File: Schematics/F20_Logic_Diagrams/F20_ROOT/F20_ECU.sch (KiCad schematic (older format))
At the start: 2 parts

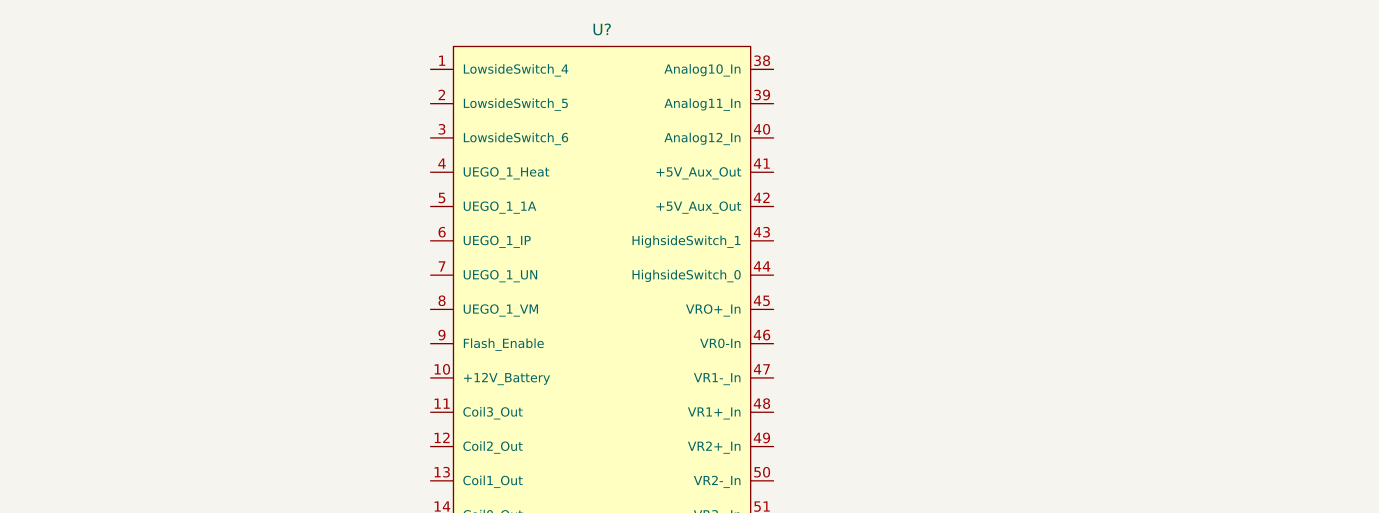
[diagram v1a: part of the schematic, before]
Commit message: Weekly update. Added Tire temp sensors drawing.
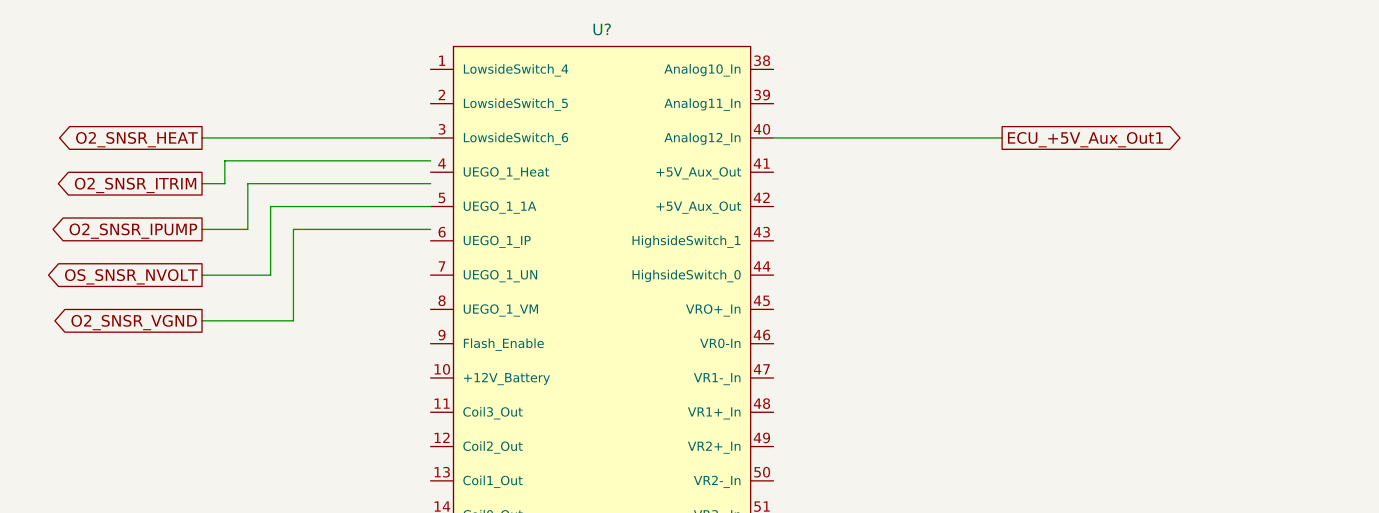
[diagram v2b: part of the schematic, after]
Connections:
- net labels added: ECU_+5V_Aux_Out1, O2_SNSR_HEAT, O2_SNSR_IPUMP, O2_SNSR_ITRIM, O2_SNSR_VGND, OS_SNSR_NVOLT
- wire segments 0 -> 14
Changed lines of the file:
@@
 EESchema Schematic File Version 4
+LIBS:F20_ROOT-cache
 EELAYER 30 0
 EELAYER END
 $Descr A4 11693 8268
 encoding utf-8
-Sheet 3 9
+Sheet 3 10
 Title ""
 Date ""
@@
 	1    0    0    -1
 $EndComp
+Text GLabel 5000 1800 2    50   Output ~ 0
+ECU_+5V_Aux_Out1
+Wire Wire Line
+	4000 1800 5000 1800
+Text GLabel 1500 1800 0    50   Output ~ 0
+O2_SNSR_HEAT
+Wire Wire Line
+	1500 1800 2500 1800
+Text GLabel 1500 2400 0    50   Output ~ 0
+OS_SNSR_NVOLT
+Text GLabel 1500 2000 0    50   Output ~ 0
+O2_SNSR_ITRIM
+Wire Wire Line
+	1500 2000 1600 2000
+Wire Wire Line
+	1600 2000 1600 1900
+Wire Wire Line
+	1600 1900 2500 1900
+Text GLabel 1500 2200 0    50   Output ~ 0
+O2_SNSR_IPUMP
+Wire Wire Line
+	1500 2200 1700 2200
+Wire Wire Line
+	1700 2200 1700 2000
+Wire Wire Line
+	1700 2000 2500 2000
+Wire Wire Line
+	1500 2400 1800 2400
+Wire Wire Line
+	1800 2400 1800 2100
+Wire Wire Line
+	1800 2100 2500 2100
+Text GLabel 1500 2600 0    50   Output ~ 0
+O2_SNSR_VGND
+Wire Wire Line
+	1500 2600 1900 2600
+Wire Wire Line
+	1900 2600 1900 2200
+Wire Wire Line
+	1900 2200 2500 2200
 $EndSCHEMATC
